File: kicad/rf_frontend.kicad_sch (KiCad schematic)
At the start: 5 parts, among them U10 LTC2311-16

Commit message: updates
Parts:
- added R20: 1K, symbol Device:R_US
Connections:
- net +2V5: now also R20.2
- net at U10.10 (~{CMOS}/LVDS): now also R20.1
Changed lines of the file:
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@@
   (junction (at 241.3 111.76) (diameter 0) (color 0 0 0 0)
   )
+  (junction (at 306.07 111.76) (diameter 0) (color 0 0 0 0)
+  )
+  (wire (pts (xy 304.8 144.78) (xy 306.07 144.78))
+    (stroke (width 0) (type default))
+  )
+  (wire (pts (xy 293.37 144.78) (xy 297.18 144.78))
+    (stroke (width 0) (type default))
+  )
   (wire (pts (xy 257.81 144.78) (xy 242.57 144.78))
     (stroke (width 0) (type default))
   )
+  (wire (pts (xy 306.07 111.76) (xy 311.15 111.76))
+    (stroke (width 0) (type default))
+  )
   (wire (pts (xy 226.06 142.24) (xy 226.06 146.05))
     (stroke (width 0) (type default))
@@
     (stroke (width 0) (type default))
   )
-  (wire (pts (xy 293.37 129.54) (xy 304.8 129.54))
-    (stroke (width 0) (type default))
-  )
-  (bus (pts (xy 214.63 137.16) (xy 214.63 138.43))
+  (wire (pts (xy 99.06 134.62) (xy 114.3 134.62))
+    (stroke (width 0) (type default))
+  )
+  (wire (pts (xy 293.37 129.54) (xy 317.5 129.54))
+    (stroke (width 0) (type default))
+  )
+  (wire (pts (xy 214.63 132.08) (xy 257.81 132.08))
     (stroke (width 0) (type default))
   )
@@
     (stroke (width 0) (type default))
   )
-  (bus (pts (xy 257.81 137.16) (xy 214.63 137.16))
-    (stroke (width 0) (type default))
-  )
-  (bus (pts (xy 99.06 134.62) (xy 114.3 134.62))
-    (stroke (width 0) (type default))
-  )
-  (wire (pts (xy 278.13 111.76) (xy 311.15 111.76))
+  (wire (pts (xy 278.13 111.76) (xy 306.07 111.76))
     (stroke (width 0) (type default))
   )
@@
     (stroke (width 0) (type default))
   )
-  (wire (pts (xy 293.37 139.7) (xy 304.8 139.7))
+  (wire (pts (xy 306.07 111.76) (xy 306.07 144.78))
+    (stroke (width 0) (type default))
+  )
+  (wire (pts (xy 293.37 139.7) (xy 317.5 139.7))
     (stroke (width 0) (type default))
   )
@@
     (stroke (width 0) (type default))
   )
-  (wire (pts (xy 293.37 137.16) (xy 304.8 137.16))
+  (wire (pts (xy 293.37 137.16) (xy 317.5 137.16))
+    (stroke (width 0) (type default))
+  )
+  (wire (pts (xy 214.63 137.16) (xy 257.81 137.16))
     (stroke (width 0) (type default))
   )
@@
     (stroke (width 0) (type default))
   )
-  (wire (pts (xy 293.37 124.46) (xy 304.8 124.46))
-    (stroke (width 0) (type default))
-  )
-  (bus (pts (xy 256.54 132.08) (xy 214.63 132.08))
+  (wire (pts (xy 293.37 124.46) (xy 317.5 124.46))
     (stroke (width 0) (type default))
   )
@@
     (stroke (width 0) (type default))
   )
-  (bus (pts (xy 214.63 130.81) (xy 214.63 132.08))
-    (stroke (width 0) (type default))
-  )
-  (wire (pts (xy 293.37 132.08) (xy 304.8 132.08))
+  (wire (pts (xy 293.37 132.08) (xy 317.5 132.08))
     (stroke (width 0) (type default))
   )
@@
     (effects (font (size 2 2)) (justify left bottom))
   )
-  (global_label "ADC_DAT_N" (shape output) (at 304.8 139.7 0) (fields_autoplaced)
-    (effects (font (size 1.27 1.27)) (justify left))
-    (property "Intersheetrefs" "${INTERSHEET_REFS}" (at 318.0057 139.7 0)
-      (effects (font (size 1.27 1.27)) (justify left) hide)
-    )
-  )
-  (global_label "ADC_SCK_P" (shape output) (at 304.8 129.54 0) (fields_autoplaced)
-    (effects (font (size 1.27 1.27)) (justify left))
-    (property "Intersheetrefs" "${INTERSHEET_REFS}" (at 318.3685 129.54 0)
-      (effects (font (size 1.27 1.27)) (justify left) hide)
-    )
-  )
-  (global_label "ADC_DAT_P" (shape output) (at 304.8 137.16 0) (fields_autoplaced)
-    (effects (font (size 1.27 1.27)) (justify left))
-    (property "Intersheetrefs" "${INTERSHEET_REFS}" (at 317.9452 137.16 0)
+  (global_label "ADC_DAT_N" (shape output) (at 317.5 139.7 0) (fields_autoplaced)
+    (effects (font (size 1.27 1.27)) (justify left))
+    (property "Intersheetrefs" "${INTERSHEET_REFS}" (at 330.7057 139.7 0)
+      (effects (font (size 1.27 1.27)) (justify left) hide)
+    )
+  )
+  (global_label "ADC_SCK_P" (shape output) (at 317.5 129.54 0) (fields_autoplaced)
+    (effects (font (size 1.27 1.27)) (justify left))
+    (property "Intersheetrefs" "${INTERSHEET_REFS}" (at 331.0685 129.54 0)
+      (effects (font (size 1.27 1.27)) (justify left) hide)
+    )
+  )
+  (global_label "ADC_DAT_P" (shape output) (at 317.5 137.16 0) (fields_autoplaced)
+    (effects (font (size 1.27 1.27)) (justify left))
+    (property "Intersheetrefs" "${INTERSHEET_REFS}" (at 330.6452 137.16 0)
       (effects (font (size 1.27 1.27)) (justify left) hide)
     )
@@
     )
   )
-  (global_label "ADC_CNV" (shape input) (at 304.8 124.46 0) (fields_autoplaced)
-    (effects (font (size 1.27 1.27)) (justify left))
-    (property "Intersheetrefs" "${INTERSHEET_REFS}" (at 316.0705 124.46 0)
-      (effects (font (size 1.27 1.27)) (justify left) hide)
-    )
-  )
-  (global_label "ADC_SCK_N" (shape output) (at 304.8 132.08 0) (fields_autoplaced)
-    (effects (font (size 1.27 1.27)) (justify left))
-    (property "Intersheetrefs" "${INTERSHEET_REFS}" (at 318.429 132.08 0)
+  (global_label "ADC_CNV" (shape input) (at 317.5 124.46 0) (fields_autoplaced)
+    (effects (font (size 1.27 1.27)) (justify left))
+    (property "Intersheetrefs" "${INTERSHEET_REFS}" (at 328.7705 124.46 0)
+      (effects (font (size 1.27 1.27)) (justify left) hide)
+    )
+  )
+  (global_label "ADC_SCK_N" (shape output) (at 317.5 132.08 0) (fields_autoplaced)
+    (effects (font (size 1.27 1.27)) (justify left))
+    (property "Intersheetrefs" "${INTERSHEET_REFS}" (at 331.129 132.08 0)
       (effects (font (size 1.27 1.27)) (justify left) hide)
     )
@@
         )
       )
+    )
+  )
+  (symbol (lib_id "Device:R_US") (at 300.99 144.78 90) (unit 1)
+    (in_bom yes) (on_board yes) (dnp no)
+    (property "Reference" "R20" (at 300.99 148.59 90)
+      (effects (font (size 1.27 1.27)))
+    )
+    (property "Value" "1K" (at 300.99 151.13 90)
+      (effects (font (size 1.27 1.27)))
+    )
+    (property "Footprint" "" (at 301.244 143.764 90)
+      (effects (font (size 1.27 1.27)) hide)
+    )
+    (property "Datasheet" "~" (at 300.99 144.78 0)
+      (effects (font (size 1.27 1.27)) hide)
+    )
+    (pin "1")
+    (pin "2")
+    (instances
+      (project "gpsrx"
+        (path "/c3c549bc-9d82-4b6a-bdb9-a3870905229d/927dd695-6d3e-4555-8e99-f99aa71ecefd"
+          (reference "R20") (unit 1)
+        )
+      )

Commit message: updates
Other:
- note added: "ADC SAMPLE RATE = 4.8MHz"
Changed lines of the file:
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@@
     (effects (font (size 2 2)) (justify left bottom))
+  )
+  (text "ADC SAMPLE RATE = 4.8MHz" (at 332.74 125.73 0)
+    (effects (font (size 1.27 1.27)) (justify left bottom))
   )
   (global_label "ADC_DAT_N" (shape output) (at 317.5 139.7 0) (fields_autoplaced)

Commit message: add some frontend stuff
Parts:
- added C49, C54: 1u, symbol Device:C
- added C50, C51: 10u, symbol Device:C
- added C52: .01u, symbol Device:C
- added C53: 47p, symbol Device:C
- added FB1: 1mH, symbol Device:FerriteBead
- added R62: 107K, symbol Device:R_US
- added R63: 22.1K, symbol Device:R_US
- added R64, R65: 25, symbol Device:R_US
- added R66, R67, R68: 1K, symbol Device:R_US
- added U20: DAT-31R5A-PP+, DG983-2_MNC, symbol bgelb_lib:DAT-31R5A-PP+
- added U21: GALI-39, Package_TO_SOT_SMD:SOT-89-3, symbol RF_Amplifier:GALI-39
- added U22: MAX8902BATA+T, 21-0168E_T822-1_MXM, symbol bgelb_lib:MAX8902BATA+T
- added U23: PCA9557D, Package_SO:SO-16_3.9x9.9mm_P1.27mm, symbol Interface_Expansion:PCA9557D
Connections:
- net +3.3V: now also C54.1, R67.1, R68.1, U23.16 (VDD); no longer C22.1, U10.4 (V_{DD})
- net GND: now also C50.2, C51.2, C54.2, R63.2, U20.10 (GND), U20.11 (GND), U20.12 (GND), U20.13 (GND), U20.18 (GND), U20.21 (GND), U20.4 (GND), U21.2 (GND), U22.2 (GND), U22.4 (GS), U22.9 (EP), U23.3 (A0), U23.4 (A1), U23.5 (A2), U23.8 (VSS)
- net at U10.6 (A_{IN+}): now also C53.1, R64.2
- net at U10.7 (A_{IN-}): now also C53.2, R65.2
- new net: C49.1, U20.14 (RFOUT)
- new net: C49.2, U21.1
- new net: R67.2, U23.15 (~{RESET})
- new net: FB1.2, R64.1, U21.3
- new net: R68.2, U22.3 (EN)
- new net: U20.16 (C4), U23.10 (IO3)
- new net: U20.15 (C8), U23.11 (IO4)
- new net: U20.1 (C16), U23.12 (IO5)
- new net: U20.20 (C0.5), U23.6 (IO0)
- new net: U20.19 (C1), U23.7 (IO1)
- new net: U20.17 (C2), U23.9 (IO2)
- new net: R62.2, R63.1, U22.6 (FB)
- new net: C52.1, U22.7 (BYP)
- new net: R66.1, U20.5 (LE)
- new net +5V: C50.1, U22.1 (IN)
- new net SCL_ATT: U23.1 (SCL)
- new net SDA_ATT: U23.2 (SDA)
- new net VDDA: C22.1, C51.1, C52.2, FB1.1, R62.1, R65.1, R66.2, U10.4 (V_{DD}), U20.6 (VDD), U20.9 (VDD), U22.8 (OUT)
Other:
- note added: "LPF"
- note added: "VDDA = 3.5V"
- note removed: "BPF, LNA, PGA"
- moved on the sheet: C22, C23, C24, C25, R20, U10

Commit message: frontend work
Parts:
- removed C54: 1u, symbol Device:C
- removed FB1: 1mH, symbol Device:FerriteBead
- removed R63: 22.1K, symbol Device:R_US
- removed R64, R65: 25, symbol Device:R_US
- removed R66, R67, R68: 1K, symbol Device:R_US
- removed U10: LTC2311-16, Package_SO:MSOP-16-1EP_3x4.039mm_P0.5mm_EP1.651x2.845mm, symbol Analog_ADC:LTC2311-16
- removed U20: DAT-31R5A-PP+, DG983-2_MNC, symbol bgelb_lib:DAT-31R5A-PP+
- removed U21: GALI-39, Package_TO_SOT_SMD:SOT-89-3, symbol RF_Amplifier:GALI-39
- removed U22: MAX8902BATA+T, 21-0168E_T822-1_MXM, symbol bgelb_lib:MAX8902BATA+T
- removed U23: PCA9557D, Package_SO:SO-16_3.9x9.9mm_P1.27mm, symbol Interface_Expansion:PCA9557D
- added C56: 1u, symbol Device:C
- added L1, L2, L3, L4: 3.6u, symbol Device:L
- added L5, L7: 3.9u, symbol Device:L
- added L6: 4.3u, symbol Device:L
- added U10: LTC6401CUD-20-PBF, QFN-16_UD_LIT, symbol bgelb_lib:LTC6401CUD-20-PBF
- added U20: PE43711B-Z, QFN24_4X4_PSM, symbol bgelb_lib:PE43711B-Z
- added U21: LTC2386CUH-16-PBF, UH_32_ADI, symbol bgelb_lib:LTC2386CUH-16-PBF
- C22: value 1u -> 600p
- C24: value 10u -> 1n
- C25: value 10u -> 600p
- C49: value 1u -> 2.2n
- C50: value 10u -> 2.2n
- C51: value 10u -> 1.3n
- C52: value .01u -> 1.3n
- C53: value 47p -> 1u
- R20: value 1K -> 29
- R62: value 107K -> 66.5
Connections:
- net +2V5: now also U21.22 (OVDD); no longer R20.2
- net ADC_CNV: now also U21.27 (CNV)
- net ADC_DAT_N: now also U21.17 (DA)
- net ADC_DAT_P: now also U21.18 (DA+)
- net ADC_SCK_N: now also U21.23 (CLK)
- net ADC_SCK_P: now also U21.24 (CLK+)
- net GND: now also C49.2, C52.2, R20.2, R62.2, U21.1 (GND), U21.10 (GND), U21.4 (GND); no longer C22.2, C24.2, C25.2
- net RF_IN: now also C52.1, L5.1
- net at C25.1: now also L1.2, U21.2 (IN+)
- net at C53.2: now also U10.13 (+IN), U10.14 (+IN)
- net at C49.1: now also L5.2, L6.1
- net at C53.1: now also R62.1, U20.14 (RF2)
- net at C24.1: now also L1.1, L3.2
- net at R20.1: now also C56.1
- net +5V: no longer names the net of C50.1
- net +5V: now also L6.2, L7.1
- removed net VDDA: C22.1, C51.1, C52.2, R62.1
- new net: C56.2, U10.15 (-IN), U10.16 (-IN)
- new net: C22.2, L4.1, U10.5 (-OUT), U10.6 (-OUTF)
- new net: C22.1, L3.1, U10.7 (+OUTF), U10.8 (+OUT)
- new net: C24.2, L2.1, L4.2
- new net: C51.1, L7.2, U20.5 (RF1)
- new net: C25.2, L2.2, U21.3 (IN)
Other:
- note added: "+20dB"
- note added: "ADC SAMPLE RATE = 9.6MHz"
- note added: "CUTOFF = 3MHz -30dB = 4.1MHz -70dB = 7.1MHz"
- note added: "CUTOFF = 3MHz -30dB = 5.6MHz"
- note removed: "ADC SAMPLE RATE = 4.8MHz"
- note removed: "LPF"
- note removed: "VDDA = 3.5V"
- moved on the sheet: C23

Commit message: power and frontend updates
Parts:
- removed U10: LTC6401CUD-20-PBF, QFN-16_UD_LIT, symbol bgelb_lib:LTC6401CUD-20-PBF
- added C54: 91p, symbol Device:C
- added C55: 430p, symbol Device:C
- added C57: 300p, symbol Device:C
- added C58, C60: 180p, symbol Device:C
- added C59, C61: 560p, symbol Device:C
- added C62, C63, C64: 1u, symbol Device:C
- added R63, R64: 49.9, symbol Device:R_US
- added TR1: ADT4-6, RF_Mini-Circuits:Mini-Circuits_CD637_H5.23mm, symbol Transformer:ADT4-6
- added U10: AD8350ARZ20-REEL7, R_8_ADI, symbol bgelb_lib:AD8350ARZ20-REEL7
- C22: value 600p -> 1.1n
- C24: value 1n -> 1.6n
- C25: value 600p -> 820p
- C49, C50: value 2.2n -> 1.8n
- C51: value 1.3n -> 1n
- C52: value 1.3n -> 1.2n
- L1, L2: value 3.6u -> 2.4u
- L3, L4: value 3.6u -> 3.3u
- L5: value 3.9u -> 3.6u
- L6: value 4.3u -> 3u
- L7: value 3.9u -> 3u
- R20: value 29 -> 49.9
- R62: value 66.5 -> 49.9
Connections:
- net GND: now also C64.2, TR1.1; no longer R20.2, R62.2
- net RF_IN: now also C54.1
- net at C53.2: now also U10.1 (IN+)
- net at C56.2: now also U10.8 (IN-)
- net at C22.2, L4.1: now also R62.2, C60.1
- net at C22.1, L3.1: now also R20.2, C58.1
- net at C24.2, L2.1, L4.2: now also C60.2, C61.1
- net at C50.1, L6.2, L7.1: now also C55.2, C57.1
- net at C51.1, L7.2, U20.5 (RF1): now also C57.2
- net at C25.1, L1.2: now also C59.2, C62.1; no longer U21.2 (IN+)
- net at C25.2, L2.2: now also C61.2, C63.1; no longer U21.3 (IN)
- net at U21.32 (VCM): now also C64.1, R63.1, R64.1
- net at C56.1: now also TR1.6; no longer R20.1
- net at C24.1, L1.1, L3.2: now also C58.2, C59.1
- net at C49.1, L5.2, L6.1: now also C54.2, C55.1
- new net: C62.2, R63.2, U21.2 (IN+)
- new net: C63.2, R64.2, U21.3 (IN)
- new net: R20.1, U10.4 (OUT+)
- new net: C53.1, TR1.4
- new net: TR1.3, U20.14 (RF2)
- new net: R62.1, U10.5 (OUT-)
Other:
- note added: "CUTOFF = 3MHz -40dB = 4.2MHz"
- note added: "CUTOFF = 3MHz -70dB = 4.8MHz -80dB = 5MHz"
- note removed: "CUTOFF = 3MHz -30dB = 4.1MHz -70dB = 7.1MHz"
- note removed: "CUTOFF = 3MHz -30dB = 5.6MHz"
- moved on the sheet: C22, C23, C24, C25, C53, C56, L1, L2, L3, L4, U20, U21

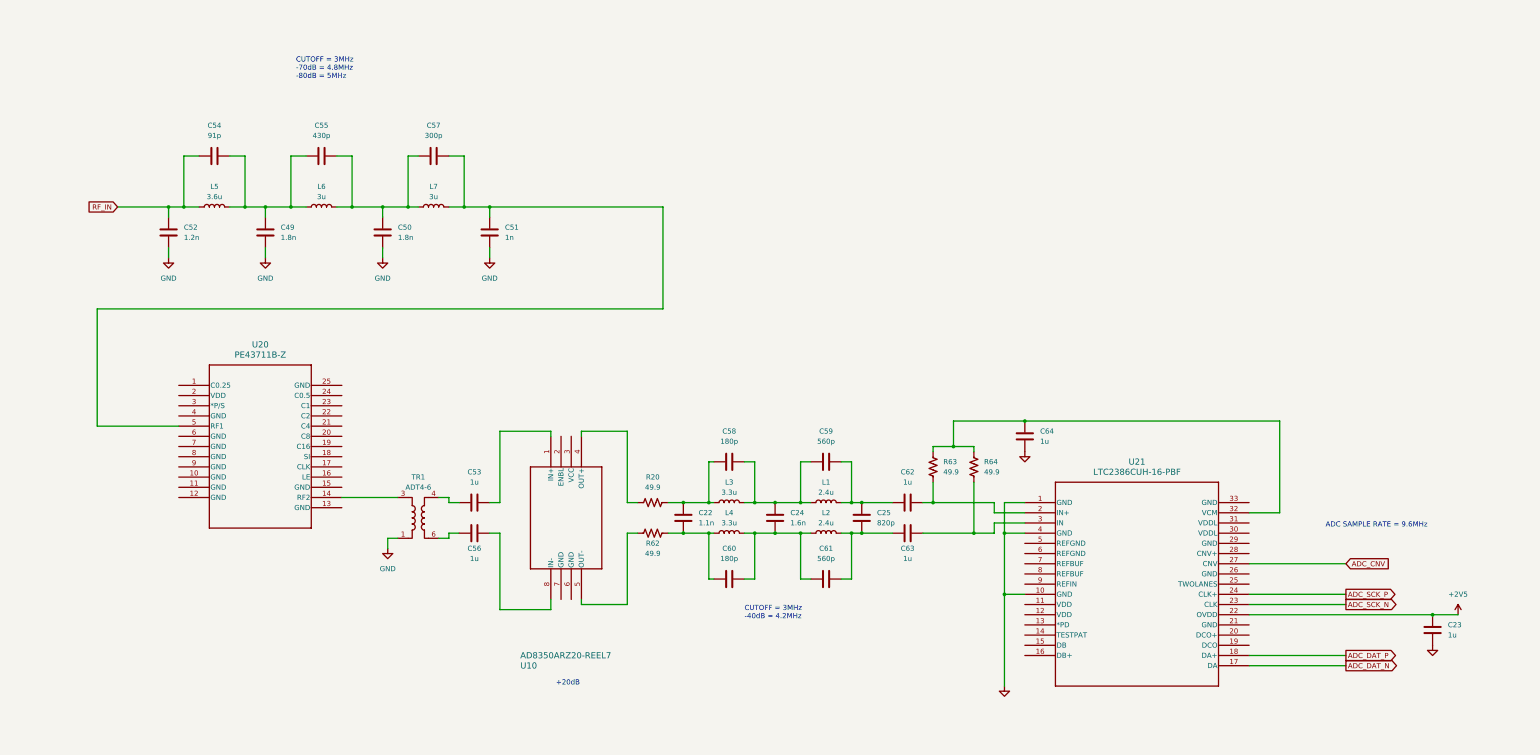
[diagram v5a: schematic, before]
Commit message: add triton t20, finish power connections
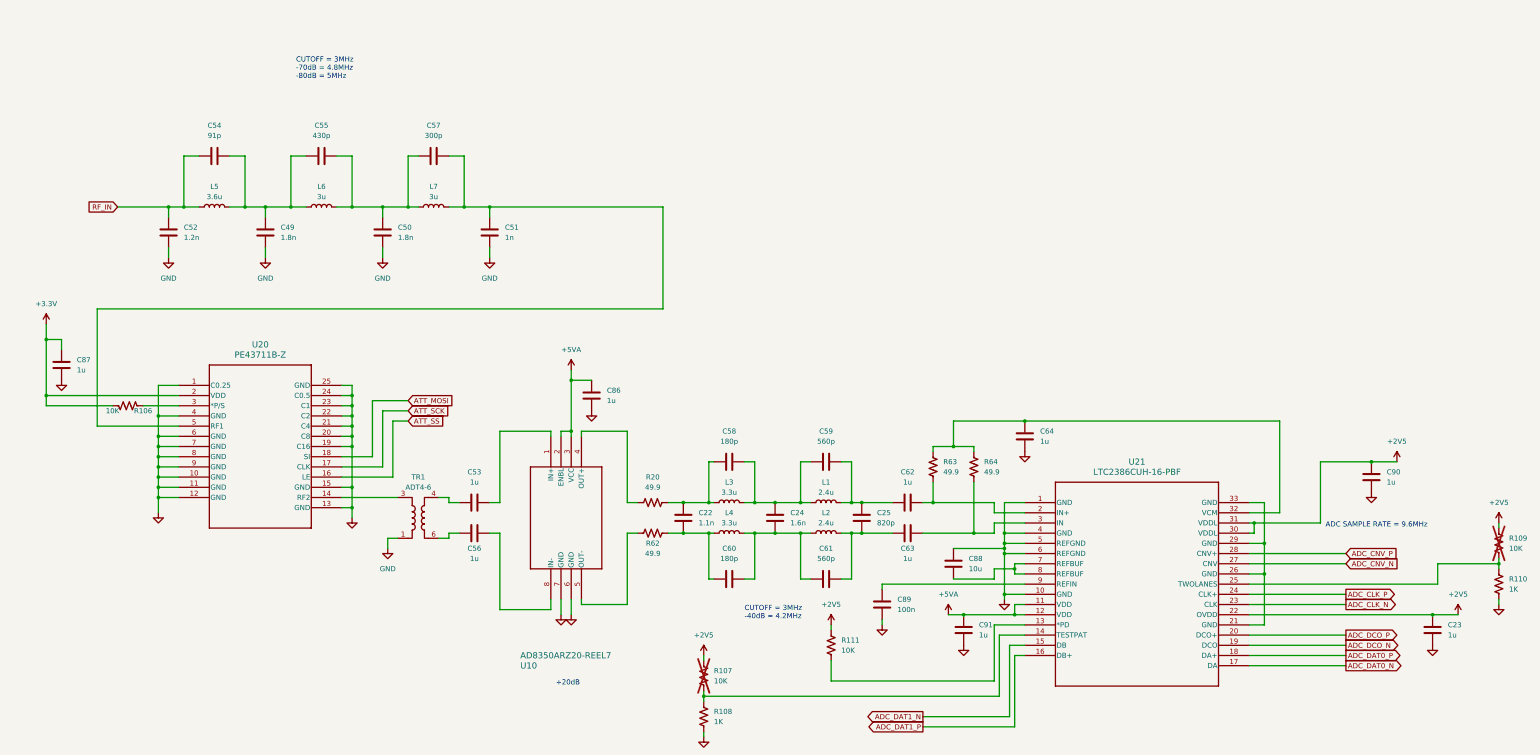
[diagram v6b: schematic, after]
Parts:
- added C86, C87, C90, C91: 1u, symbol Device:C
- added C88: 10u, symbol Device:C
- added C89: 100n, symbol Device:C
- added R106, R107, R109, R111: 10K, symbol Device:R_US
- added R108, R110: 1K, symbol Device:R_US
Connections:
- net +2V5: now also U21.30 (VDDL), U21.31 (VDDL), C90.1, R107.1, R109.1, R111.1
- net GND: now also U10.6 (GND), U10.7 (GND), U20.1 (C0.25), U20.10 (GND), U20.11 (GND), U20.12 (GND), U20.13 (GND), U20.15 (GND), U20.19 (C16), U20.20 (C8), U20.21 (C4), U20.22 (C2), U20.23 (C1), U20.24 (C0.5), U20.25 (GND), U20.4 (GND), U20.6 (GND), U20.7 (GND), U20.8 (GND), U20.9 (GND), U21.5 (REFGND), U21.6 (REFGND), C86.2, C87.2, C88.1, C89.2, C90.2, C91.2, R108.2, R110.2
- net +5VA: now reaches U21.11 (VDD)
- net +5VA: now also U10.2 (ENBL), U10.3 (VCC), U21.12 (VDD), C86.1, C91.1
- net at U21.13 (*PD): now also R111.2
- net at U21.14 (TESTPAT): now also R107.2, R108.1
- net ADC_DAT1_N: now reaches U21.15 (DB)
- net ADC_DAT1_P: now reaches U21.16 (DB+)
- net ADC_DCO_N: now reaches U21.19 (DCO)
- net ADC_DCO_P: now reaches U21.20 (DCO+)
- net at U21.21 (GND): now also U21.26 (GND), U21.29 (GND), U21.33 (GND)
- net at U21.25 (TWOLANES): now also R109.2, R110.1
- net ADC_CNV_P: now reaches U21.28 (CNV+)
- net at U21.7 (REFBUF): now also U21.8 (REFBUF), C88.2
- net at U21.9 (REFIN): now also C89.1
- net ATT_SS: now reaches U20.16 (LE)
- net ATT_SCK: now reaches U20.17 (CLK)
- net ATT_MOSI: now reaches U20.18 (SI)
- net +3.3V: now reaches U20.2 (VDD)
- net +3.3V: now also C87.1, R106.2
- net at U20.3 (*P/S): now also R106.1
- net ADC_CNV renamed ADC_CNV_N
- net ADC_DAT_N renamed ADC_DAT0_N
- net ADC_DAT_P renamed ADC_DAT0_P
- net ADC_SCK_N renamed ADC_CLK_N
- net ADC_SCK_P renamed ADC_CLK_P

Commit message: assign footprints
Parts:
- added D1, D2, D3, D4: 1N4448W, Diode_SMD:D_SOD-123, symbol Diode:1N4448W
- C22, C24, C25, C49, C50, C51, C52, C54, C55, C57, C58, C59, C60, C61, C88: footprint (none) -> Capacitor_SMD:C_0805_2012Metric_Pad1.18x1.45mm_HandSolder
- C23, C53, C56, C62, C63, C64, C86, C87, C89, C90, C91: footprint (none) -> Capacitor_SMD:C_0603_1608Metric_Pad1.08x0.95mm_HandSolder
- L1, L2, L3, L4, L5, L6, L7: footprint (none) -> Inductor_SMD:L_1812_4532Metric_Pad1.30x3.40mm_HandSolder
- R106, R107, R108, R109, R110, R111, R20, R62, R63, R64: footprint (none) -> Resistor_SMD:R_0603_1608Metric_Pad0.98x0.95mm_HandSolder
- U10: footprint R_8_ADI -> bgelb_footprint:SOIC127P600X175-8N
- U20: footprint QFN24_4X4_PSM -> bgelb_footprint:QFN24_4X4_PSM
- U21: footprint UH_32_ADI -> bgelb_footprint:UH_32_ADI
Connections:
- net GND: now also D2.1 (K), D4.2 (A)
- net RF_IN: now also D1.2 (A), D3.1 (K)
- new net: D1.1 (K), D2.2 (A)
- new net: D3.2 (A), D4.1 (K)

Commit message: fix ercs
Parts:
- added R130: 1K, Resistor_SMD:R_0603_1608Metric_Pad0.98x0.95mm_HandSolder, symbol Device:R_US
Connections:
- net GND: now also U21.21 (GND), U21.26 (GND), U21.29 (GND), U21.33 (GND), R130.2; no longer U20.1 (C0.25), U20.19 (C16), U20.20 (C8), U20.21 (C4), U20.22 (C2), U20.23 (C1), U20.24 (C0.5)
- new net: R130.1, U20.1 (C0.25), U20.19 (C16), U20.20 (C8), U20.21 (C4), U20.22 (C2), U20.23 (C1), U20.24 (C0.5)
